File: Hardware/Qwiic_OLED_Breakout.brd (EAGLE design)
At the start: 27.3 x 29.7 mm, 45 parts, among them J1 QWIIC_RIGHT_ANGLE, J2 QWIIC_RIGHT_ANGLE

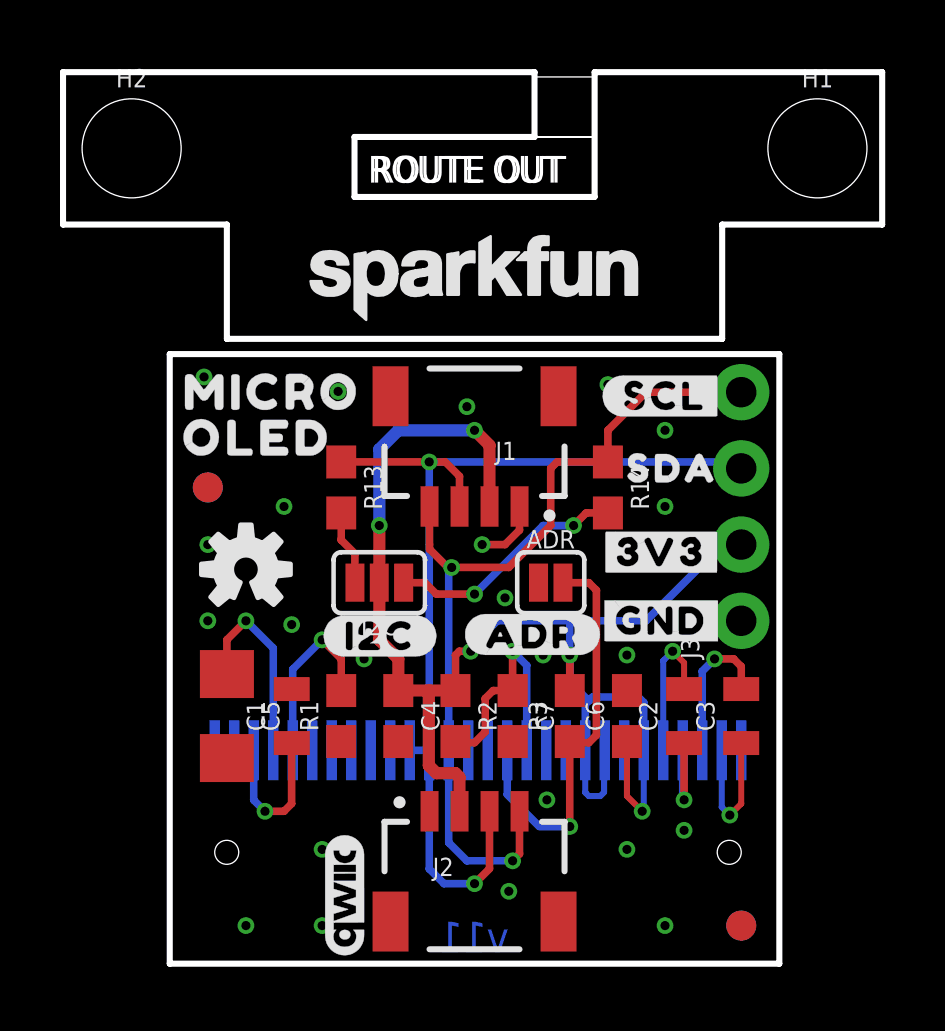
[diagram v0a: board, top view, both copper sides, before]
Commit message: Fixes mounting hole spacing (derp)
* Adds more measures
* Changes pull up resistor values
* Fixes some notes on ordering instructions
* Adds more notes and silk
* Connects some GND pour
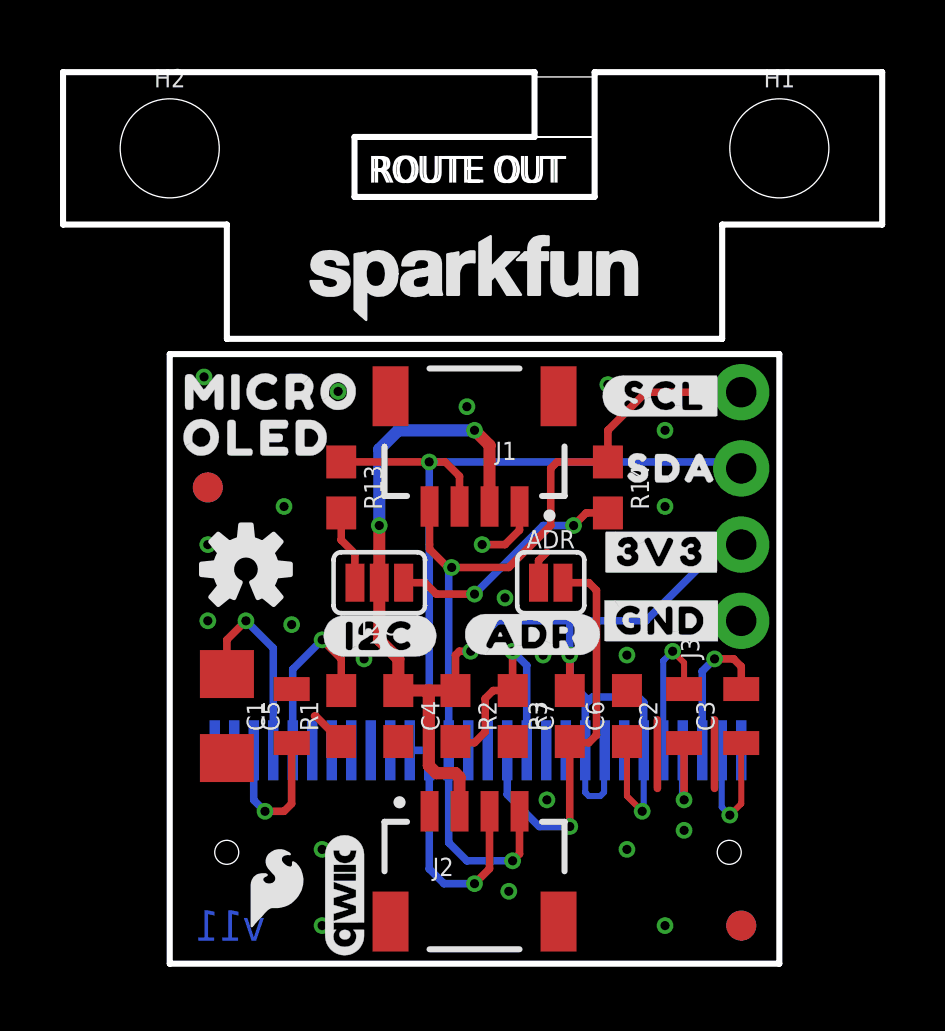
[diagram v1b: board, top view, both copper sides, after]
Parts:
- added U$15: (no value), SparkFun-Aesthetics:SFE_LOGO_FLAME_.1
- R13, R14: value 4.7k -> 2.2k
- moved H2 1.27 mm to (0.00, 27.2)
- moved H1 1.27 mm to (20.3, 27.2)
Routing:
- net GND: track 2.23 -> 9.18 mm, vias 23 -> 22
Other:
- board text added: "Red Soldermask"
- board text removed: "Red Silk"
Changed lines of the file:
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@@
 <layer number="154" name="FabDoc2" color="7" fill="1" visible="no" active="yes"/>
 <layer number="155" name="FabDoc3" color="7" fill="1" visible="no" active="yes"/>
-<layer number="156" name="gesam-Maß" color="7" fill="1" visible="yes" active="yes"/>
-<layer number="157" name="FaceMchng" color="7" fill="1" visible="yes" active="yes"/>
-<layer number="158" name="FaceMMeas" color="7" fill="1" visible="yes" active="yes"/>
-<layer number="159" name="Geh-Bear2" color="7" fill="1" visible="yes" active="yes"/>
-<layer number="160" name="Topologie" color="7" fill="1" visible="yes" active="yes"/>
-<layer number="161" name="tomplace2" color="7" fill="1" visible="yes" active="yes"/>
+<layer number="156" name="gesam-Maß" color="7" fill="1" visible="no" active="yes"/>
+<layer number="157" name="FaceMchng" color="7" fill="1" visible="no" active="yes"/>
+<layer number="158" name="FaceMMeas" color="7" fill="1" visible="no" active="yes"/>
+<layer number="159" name="Geh-Bear2" color="7" fill="1" visible="no" active="yes"/>
+<layer number="160" name="Topologie" color="7" fill="1" visible="no" active="yes"/>
+<layer number="161" name="tomplace2" color="7" fill="1" visible="no" active="yes"/>
 <layer number="166" name="AntennaArea" color="7" fill="1" visible="no" active="no"/>
 <layer number="168" name="4mmHeightArea" color="7" fill="1" visible="no" active="no"/>
@@
 <layer number="250" name="Descript" color="7" fill="1" visible="no" active="yes"/>
 <layer number="251" name="SMDround" color="7" fill="1" visible="no" active="yes"/>
-<layer number="252" name="BR-BS" color="7" fill="1" visible="yes" active="yes"/>
+<layer number="252" name="BR-BS" color="7" fill="1" visible="no" active="yes"/>
 <layer number="253" name="Extra" color="7" fill="1" visible="no" active="no"/>
 <layer number="254" name="cooling" color="7" fill="1" visible="no" active="yes"/>
@@
 <board>
 <plain>
-<text x="11.303" y="0.381" size="1.016" layer="16" font="vector" ratio="20" rot="MR0">v11</text>
+<text x="3.175" y="0.762" size="1.016" layer="16" font="vector" ratio="20" rot="MR0">v11</text>
 <wire x1="20.32" y1="0" x2="20.32" y2="20.32" width="0.2032" layer="20"/>
 <wire x1="0" y1="20.32" x2="0" y2="0" width="0.2032" layer="20"/>
@@
 <wire x1="18.415" y1="20.828" x2="18.415" y2="24.638" width="0.2032" layer="20"/>
 <wire x1="0" y1="20.32" x2="20.32" y2="20.32" width="0.2032" layer="20"/>
-<dimension x1="-1.27" y1="27.178" x2="21.59" y2="27.178" x3="10.16" y3="36.83" textsize="1.778" layer="47" unit="inch"/>
 <text x="6.731" y="26.035" size="0.889" layer="46" font="vector" ratio="12">ROUTE OUT</text>
 <text x="6.604" y="26.035" size="0.889" layer="46" font="vector" ratio="12">ROUTE OUT</text>
@@
 <dimension x1="0" y1="0" x2="20.32" y2="0" x3="10.16" y3="-10.16" textsize="1.778" textratio="12" layer="47" unit="inch"/>
 <dimension x1="10.16" y1="5.08" x2="0" y2="5.08" x3="5.08" y3="-5.08" textsize="1.778" textratio="12" layer="47" unit="inch"/>
-<dimension x1="-1.27" y1="27.178" x2="0" y2="20.32" x3="-0.635" y3="33.02" textsize="1.778" textratio="12" layer="47" dtype="horizontal" unit="inch"/>
 <text x="-26.67" y="-6.35" size="1.778" layer="47" font="vector" ratio="12">Units in Inches</text>
 <text x="31.75" y="34.29" size="1.778" layer="51" font="vector" ratio="12">Two Layer Board</text>
-<text x="31.75" y="31.75" size="1.778" layer="51" font="vector" ratio="12">Red Silk</text>
+<text x="31.75" y="31.75" size="1.778" layer="51" font="vector" ratio="12">Red Soldermask</text>
 <text x="31.75" y="29.21" size="1.778" layer="51" font="vector" ratio="12">White Silkscreen</text>
 <text x="31.75" y="26.67" size="1.778" layer="51" font="vector" ratio="12">1.6mm Thickness</text>
 <text x="31.75" y="24.13" size="1.778" layer="51" font="vector" ratio="12">Lead-Free HASL</text>
+<dimension x1="0" y1="27.178" x2="20.32" y2="27.178" x3="10.16" y3="34.29" textsize="1.778" textratio="15" layer="47" unit="inch"/>
+<dimension x1="20.32" y1="0" x2="20.32" y2="11.43" x3="26.67" y3="5.715" textsize="1.778" textratio="15" layer="47" unit="inch"/>
+<dimension x1="20.32" y1="0" x2="20.32" y2="19.05" x3="31.75" y3="9.525" textsize="1.778" textratio="15" layer="47" unit="inch"/>
 </plain>
 <attributes>
@@
 <attribute name="VALUE" x="8.763" y="8.255" size="0.6096" layer="27" font="vector" ratio="20" rot="R270" align="top-center"/>
 </element>
-<element name="R13" library="SparkFun-Resistors" package="0603" value="4.7k" x="5.715" y="15.875" smashed="yes" rot="R270">
+<element name="R13" library="SparkFun-Resistors" package="0603" value="2.2k" x="5.715" y="15.875" smashed="yes" rot="R270">
 <attribute name="NAME" x="6.477" y="15.875" size="0.6096" layer="25" font="vector" ratio="20" rot="R270" align="bottom-center"/>
-<attribute name="PROD_ID" value="RES-07857" x="5.715" y="15.875" size="1.778" layer="27" font="vector" ratio="15" rot="R270" display="off"/>
-<attribute name="VALUE" x="4.953" y="15.875" size="0.6096" layer="27" font="vector" ratio="20" rot="R270" align="top-center"/>
-</element>
-<element name="R14" library="SparkFun-Resistors" package="0603" value="4.7k" x="14.605" y="15.875" smashed="yes" rot="R270">
+<attribute name="PROD_ID" value="RES-08272" x="5.715" y="15.875" size="1.778" layer="27" font="vector" ratio="15" rot="R270" display="off"/>
+<attribute name="VALUE" value="2.2k" x="4.953" y="15.875" size="0.6096" layer="27" font="vector" ratio="20" rot="R270" align="top-center"/>
+</element>
+<element name="R14" library="SparkFun-Resistors" package="0603" value="2.2k" x="14.605" y="15.875" smashed="yes" rot="R270">
 <attribute name="NAME" x="15.367" y="15.875" size="0.6096" layer="25" font="vector" ratio="20" rot="R270" align="bottom-center"/>
-<attribute name="PROD_ID" value="RES-07857" x="14.605" y="15.875" size="1.778" layer="27" font="vector" ratio="15" rot="R270" display="off"/>
-<attribute name="VALUE" x="13.843" y="15.875" size="0.6096" layer="27" font="vector" ratio="20" rot="R270" align="top-center"/>
+<attribute name="PROD_ID" value="RES-08272" x="14.605" y="15.875" size="1.778" layer="27" font="vector" ratio="15" rot="R270" display="off"/>
+<attribute name="VALUE" value="2.2k" x="13.843" y="15.875" size="0.6096" layer="27" font="vector" ratio="20" rot="R270" align="top-center"/>
 </element>
 <element name="I2C" library="SparkFun-Jumpers" package="SMT-JUMPER_3_2-NC_PASTE_SILK" package3d_urn="urn:adsk.eagle:package:39294/1" value="JUMPER-SMT_3_2-NC_PASTE_SILK" x="6.985" y="12.7" smashed="yes" rot="R180">
@@
 <attribute name="VALUE" x="6.985" y="13.843" size="0.6096" layer="27" font="vector" ratio="20" rot="R180" align="top-center"/>
 </element>
-<element name="H1" library="SparkFun-Hardware" package="STAND-OFF" value="STAND-OFF" x="21.59" y="27.178" smashed="yes">
-<attribute name="NAME" x="21.59" y="29.21" size="0.6096" layer="25" font="vector" ratio="20" align="bottom-center"/>
-<attribute name="VALUE" x="21.59" y="25.146" size="0.6096" layer="27" font="vector" ratio="20" align="top-center"/>
-</element>
-<element name="H2" library="SparkFun-Hardware" package="STAND-OFF" value="STAND-OFF" x="-1.27" y="27.178" smashed="yes">
-<attribute name="NAME" x="-1.27" y="29.21" size="0.6096" layer="25" font="vector" ratio="20" align="bottom-center"/>
-<attribute name="VALUE" x="-1.27" y="25.146" size="0.6096" layer="27" font="vector" ratio="20" align="top-center"/>
+<element name="H1" library="SparkFun-Hardware" package="STAND-OFF" value="STAND-OFF" x="20.32" y="27.178" smashed="yes">
+<attribute name="NAME" x="20.32" y="29.21" size="0.6096" layer="25" font="vector" ratio="20" align="bottom-center"/>
+<attribute name="VALUE" x="20.32" y="25.146" size="0.6096" layer="27" font="vector" ratio="20" align="top-center"/>
+</element>
+<element name="H2" library="SparkFun-Hardware" package="STAND-OFF" value="STAND-OFF" x="0" y="27.178" smashed="yes">
+<attribute name="NAME" x="0" y="29.21" size="0.6096" layer="25" font="vector" ratio="20" align="bottom-center"/>
+<attribute name="VALUE" x="0" y="25.146" size="0.6096" layer="27" font="vector" ratio="20" align="top-center"/>
 </element>
 <element name="ADR" library="SparkFun-Jumpers" package="SMT-JUMPER_2_NO_SILK" package3d_urn="urn:adsk.eagle:package:39279/1" value="JUMPER-SMT_2_NO_SILK" x="12.7" y="12.7" smashed="yes">
@@
 <element name="LOGO4" library="SparkFun-Aesthetics" package="SFE_LOGO_NAME_.1" value="SFE_LOGO_NAME.1_INCH" x="6.604" y="18.415" smashed="yes" rot="MR0"/>
 <element name="LOGO6" library="SparkFun-Aesthetics" package="ORDERING_INSTRUCTIONS" value="SPECIAL_INSTRUCTIONS-ORDERING" x="30.48" y="46.99" smashed="yes"/>
+<element name="U$15" library="SparkFun-Aesthetics" package="SFE_LOGO_FLAME_.1" value="" x="3.556" y="2.54" smashed="yes"/>
 </elements>
 <signals>
@@
 <via x="1.27" y="13.97" extent="1-16" drill="0.3048"/>
 <via x="1.27" y="11.43" extent="1-16" drill="0.3048"/>
-<via x="2.54" y="1.27" extent="1-16" drill="0.3048"/>
 <via x="16.51" y="1.27" extent="1-16" drill="0.3048"/>
 <via x="5.08" y="1.27" extent="1-16" drill="0.3048"/>
 <via x="14.605" y="19.304" extent="1-16" drill="0.3048"/>
 <via x="5.6134" y="19.0754" extent="1-16" drill="0.3048"/>
+<wire x1="12.2936" y1="12.7" x2="12.2936" y2="13.4366" width="0.254" layer="1"/>
+<wire x1="12.2936" y1="13.4366" x2="12.573" y2="13.716" width="0.254" layer="1"/>
+<wire x1="5.715" y1="7.405" x2="4.865" y2="8.255" width="0.254" layer="1"/>
+<wire x1="4.865" y1="8.255" x2="4.826" y2="8.255" width="0.254" layer="1"/>
+<wire x1="18.161" y1="5.842" x2="18.161" y2="8.128" width="0.254" layer="1"/>
+<wire x1="16.256" y1="5.842" x2="16.256" y2="8.128" width="0.254" layer="1"/>
 </signal>
 <signal name="VDD">

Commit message: Fixes some proportional text, cleans up some nets
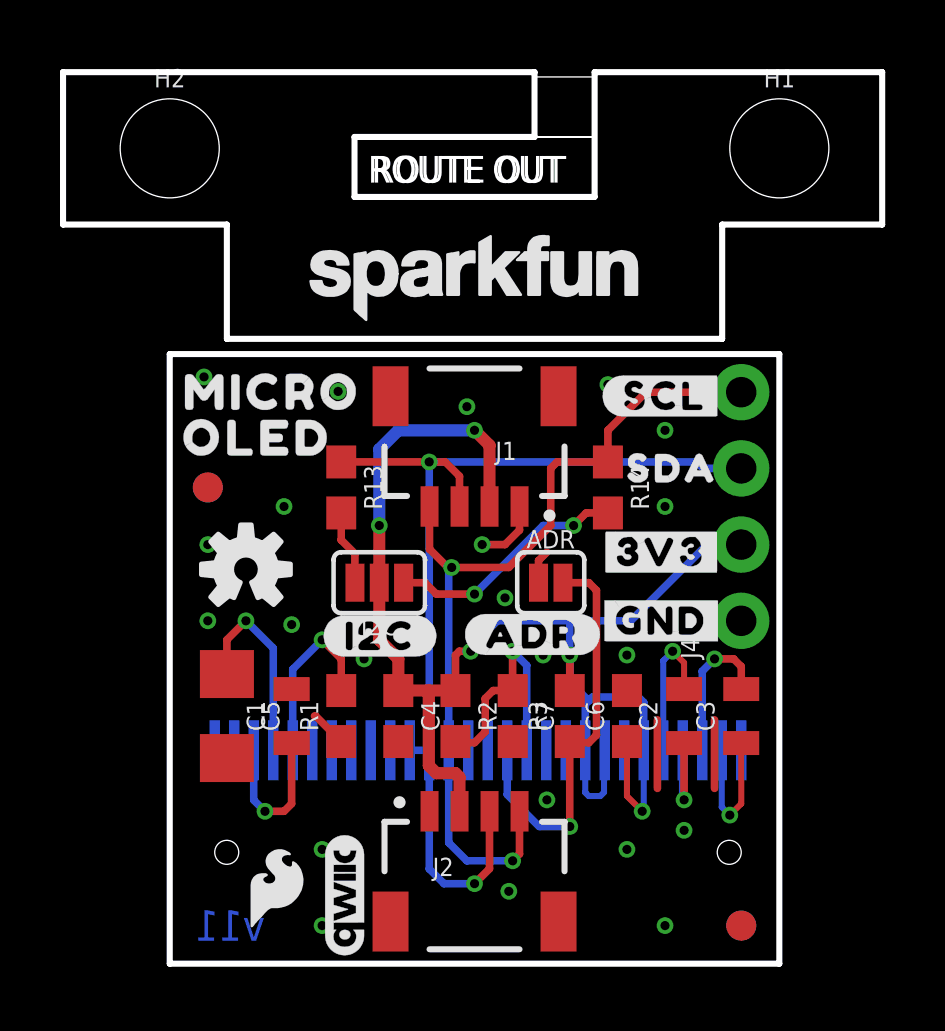
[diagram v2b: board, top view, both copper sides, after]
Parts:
- removed J3: (no value), SparkX:1X04_NO_SILK
- removed LOGO1: REVISION, SparkFun-Aesthetics:REVISION
- added J4: (no value), SparkFun-Connectors:1X04_NO_SILK
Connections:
- net D0/SCL/SCK: now also J4.4; no longer J3.4
- net D1/SDA/PICO: now also J4.3; no longer J3.3
- net GND: now also J4.1; no longer J3.1
- net VDD: now also J4.2; no longer J3.2
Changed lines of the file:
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@@
 <layer number="45" name="Holes" color="7" fill="1" visible="yes" active="yes"/>
 <layer number="46" name="Milling" color="3" fill="1" visible="no" active="yes"/>
-<layer number="47" name="Measures" color="7" fill="1" visible="yes" active="yes"/>
+<layer number="47" name="Measures" color="7" fill="1" visible="no" active="yes"/>
 <layer number="48" name="Document" color="7" fill="1" visible="no" active="yes"/>
 <layer number="49" name="Reference" color="13" fill="1" visible="yes" active="yes"/>
@@
 <attribute name="VALUE" value="QWIIC_RIGHT_ANGLE" x="8.509" y="1.778" size="0.6096" layer="27" font="vector" ratio="20"/>
 </element>
-<element name="J3" library="SparkX" package="1X04_NO_SILK" value="" x="19.05" y="11.43" smashed="yes" rot="R90">
-<attribute name="NAME" x="17.653" y="10.16" size="0.6096" layer="25" font="vector" ratio="20" rot="R90"/>
-<attribute name="VALUE" x="21.082" y="10.16" size="0.6096" layer="27" font="vector" ratio="20" rot="R90"/>
-</element>
 <element name="R3" library="SparkFun-Resistors" package="0603" value="10k" x="13.335" y="8.255" smashed="yes" rot="R90">
 <attribute name="NAME" x="12.573" y="8.255" size="0.6096" layer="25" font="vector" ratio="20" rot="R90" align="bottom-center"/>
@@
 <attribute name="VALUE" x="12.7" y="11.557" size="0.6096" layer="27" font="vector" ratio="20" align="top-center"/>
 </element>
-<element name="LOGO1" library="SparkFun-Aesthetics" package="REVISION" value="REVISION" x="-6.35" y="-30.48" smashed="yes"/>
 <element name="FID3" library="SparkFun-Aesthetics" package="FIDUCIAL-1X2" value="FIDUCIAL1X2" x="1.27" y="15.875" smashed="yes" rot="MR0"/>
 <element name="FID4" library="SparkFun-Aesthetics" package="FIDUCIAL-1X2" value="FIDUCIAL1X2" x="19.05" y="1.27" smashed="yes" rot="MR0"/>
@@
 <element name="LOGO6" library="SparkFun-Aesthetics" package="ORDERING_INSTRUCTIONS" value="SPECIAL_INSTRUCTIONS-ORDERING" x="30.48" y="46.99" smashed="yes"/>
 <element name="U$15" library="SparkFun-Aesthetics" package="SFE_LOGO_FLAME_.1" value="" x="3.556" y="2.54" smashed="yes"/>
+<element name="J4" library="SparkFun-Connectors" package="1X04_NO_SILK" value="" x="19.05" y="11.43" smashed="yes" rot="R90">
+<attribute name="NAME" x="17.653" y="10.16" size="0.6096" layer="25" font="vector" ratio="20" rot="R90"/>
+<attribute name="VALUE" x="21.082" y="10.16" size="0.6096" layer="27" font="vector" ratio="20" rot="R90"/>
+</element>
 </elements>
 <signals>
@@
 <contactref element="J1" pad="1"/>
 <contactref element="J2" pad="1"/>
-<contactref element="J3" pad="1"/>
 <contactref element="C7" pad="2"/>
 <via x="5.08" y="3.81" extent="1-16" drill="0.3048"/>
@@
 <wire x1="18.161" y1="5.842" x2="18.161" y2="8.128" width="0.254" layer="1"/>
 <wire x1="16.256" y1="5.842" x2="16.256" y2="8.128" width="0.254" layer="1"/>
+<contactref element="J4" pad="1"/>
 </signal>
 <signal name="VDD">
@@
 <contactref element="J1" pad="2"/>
 <contactref element="J2" pad="2"/>
-<contactref element="J3" pad="2"/>
 <contactref element="R3" pad="2"/>
 <contactref element="R2" pad="1"/>
@@
 <wire x1="9.652" y1="10.414" x2="10.033" y2="10.414" width="0.254" layer="1"/>
 <via x="10.033" y="10.414" extent="1-16" drill="0.3048"/>
-<wire x1="15.875" y1="11.43" x2="13.335" y2="11.43" width="0.254" layer="16"/>
-<wire x1="18.415" y1="13.97" x2="19.05" y2="13.97" width="0.254" layer="16"/>
+<wire x1="15.367" y1="11.43" x2="13.335" y2="11.43" width="0.254" layer="16"/>
 <wire x1="13.335" y1="11.43" x2="10.922" y2="11.43" width="0.254" layer="16"/>
 <wire x1="10.922" y1="11.43" x2="10.033" y2="10.541" width="0.254" layer="16"/>
 <wire x1="10.033" y1="10.414" x2="10.033" y2="10.541" width="0.254" layer="16"/>
-<wire x1="15.875" y1="11.43" x2="18.415" y2="13.97" width="0.254" layer="16"/>
+<wire x1="17.907" y1="13.97" x2="15.367" y2="11.43" width="0.254" layer="16"/>
 <contactref element="OLED1" pad="9"/>
 <wire x1="13.85" y1="8.643" x2="13.97" y2="8.763" width="0.254" layer="16"/>
@@
 <wire x1="13.335" y1="9.398" x2="13.335" y2="10.287" width="0.254" layer="16"/>
 <wire x1="13.335" y1="10.287" x2="13.335" y2="11.43" width="0.254" layer="16"/>
+<contactref element="J4" pad="2"/>
+<wire x1="19.05" y1="13.97" x2="17.907" y2="13.97" width="0.254" layer="16"/>
 </signal>
 <signal name="VCOMH">
@@
 <contactref element="J1" pad="3"/>
 <contactref element="J2" pad="3"/>
-<contactref element="J3" pad="3"/>
 <contactref element="OLED1" pad="18"/>
 <wire x1="8" y1="7.112" x2="8.65" y2="7.112" width="0.254" layer="16"/>
@@
 <contactref element="R13" pad="1"/>
 <via x="8.65" y="16.725" extent="1-16" drill="0.3048"/>
-<wire x1="8.65" y1="16.725" x2="18.835" y2="16.725" width="0.254" layer="16"/>
-<wire x1="18.835" y1="16.725" x2="19.05" y2="16.51" width="0.254" layer="16"/>
+<wire x1="8.65" y1="16.725" x2="17.565" y2="16.725" width="0.254" layer="16"/>
 <wire x1="8.65" y1="16.725" x2="9.183" y2="16.725" width="0.254" layer="1"/>
 <wire x1="9.183" y1="16.725" x2="9.66" y2="16.248" width="0.254" layer="1"/>
 <wire x1="5.715" y1="16.725" x2="8.65" y2="16.725" width="0.254" layer="1"/>
 <wire x1="9.66" y1="16.248" x2="9.66" y2="15.24" width="0.254" layer="1"/>
+<contactref element="J4" pad="3"/>
+<wire x1="19.05" y1="16.51" x2="17.78" y2="16.51" width="0.254" layer="16"/>
+<wire x1="17.78" y1="16.51" x2="17.565" y2="16.725" width="0.254" layer="16"/>
 </signal>
 <signal name="D0/SCL/SCK">
@@
 <contactref element="J1" pad="4"/>
 <contactref element="J2" pad="4"/>
-<contactref element="J3" pad="4"/>
 <wire x1="11.66" y1="5.08" x2="11.66" y2="3.659" width="0.254" layer="1"/>
 <wire x1="11.66" y1="3.659" x2="11.43" y2="3.429" width="0.254" layer="1"/>
@@
 <wire x1="9.398" y1="13.208" x2="9.271" y2="13.208" width="0.254" layer="1"/>
 <wire x1="9.271" y1="13.208" x2="8.66" y2="13.819" width="0.254" layer="1"/>
-<wire x1="19.05" y1="19.05" x2="15.875" y2="19.05" width="0.254" layer="1"/>
-<wire x1="15.875" y1="19.05" x2="14.605" y2="17.78" width="0.254" layer="1"/>
+<wire x1="14.605" y1="17.78" x2="15.875" y2="19.05" width="0.254" layer="1"/>
 <wire x1="14.605" y1="17.78" x2="14.605" y2="16.725" width="0.254" layer="1"/>
-<wire x1="8.66" y1="13.819" x2="8.66" y2="13.97" width="0.254" layer="1"/>
-<wire x1="8.66" y1="13.97" x2="8.66" y2="15.24" width="0.254" layer="1"/>
+<wire x1="8.66" y1="13.819" x2="8.66" y2="15.24" width="0.254" layer="1"/>
+<contactref element="J4" pad="4"/>
+<wire x1="15.875" y1="19.05" x2="19.05" y2="19.05" width="0.254" layer="1"/>
 </signal>
 <signal name="RESET">
